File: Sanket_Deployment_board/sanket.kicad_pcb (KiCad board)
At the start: 2 copper layers, 95.9 x 92 mm, 41 parts, among them J2 Conn_02x03_Counter_Clockwise, J3 Conn_02x03_Counter_Clockwise

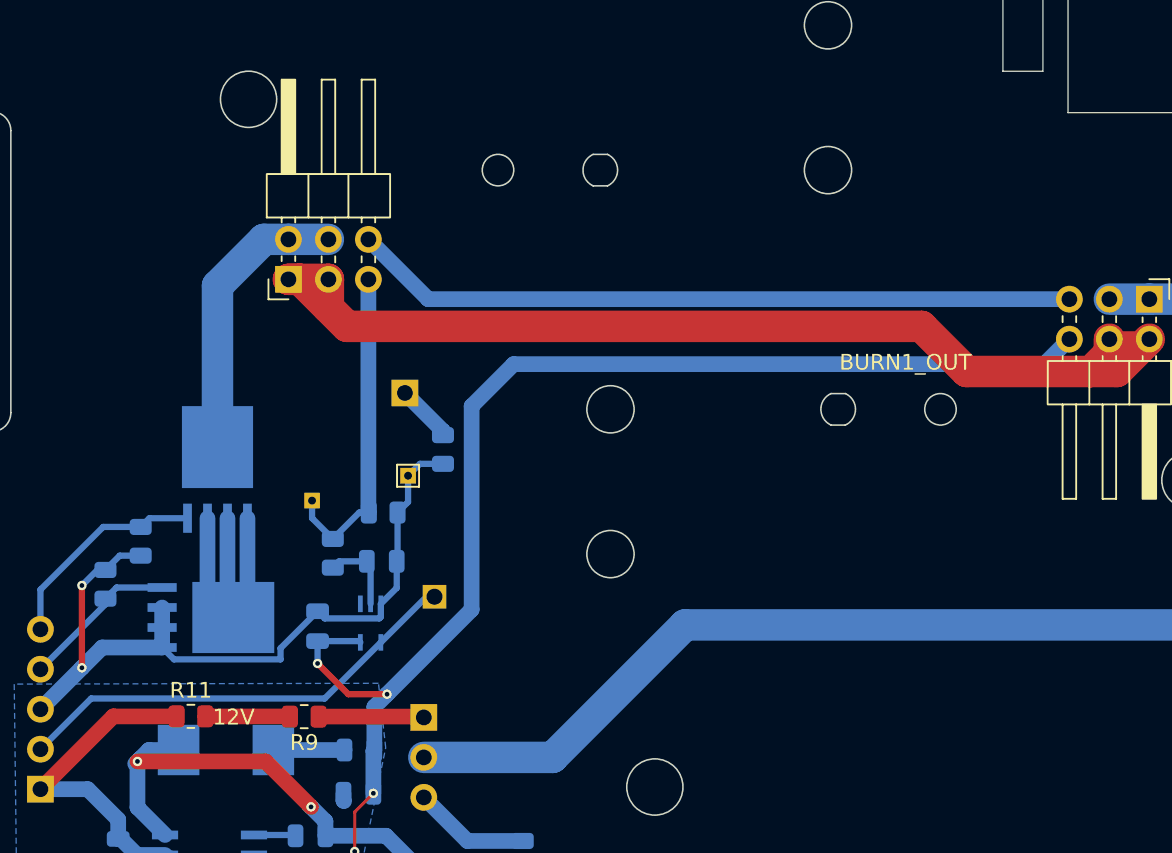
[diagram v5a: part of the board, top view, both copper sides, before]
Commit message: Added antenna bleeder, switched FIRE and ARM with each other, Corrected Schmitt trigger symbol to non-inverting
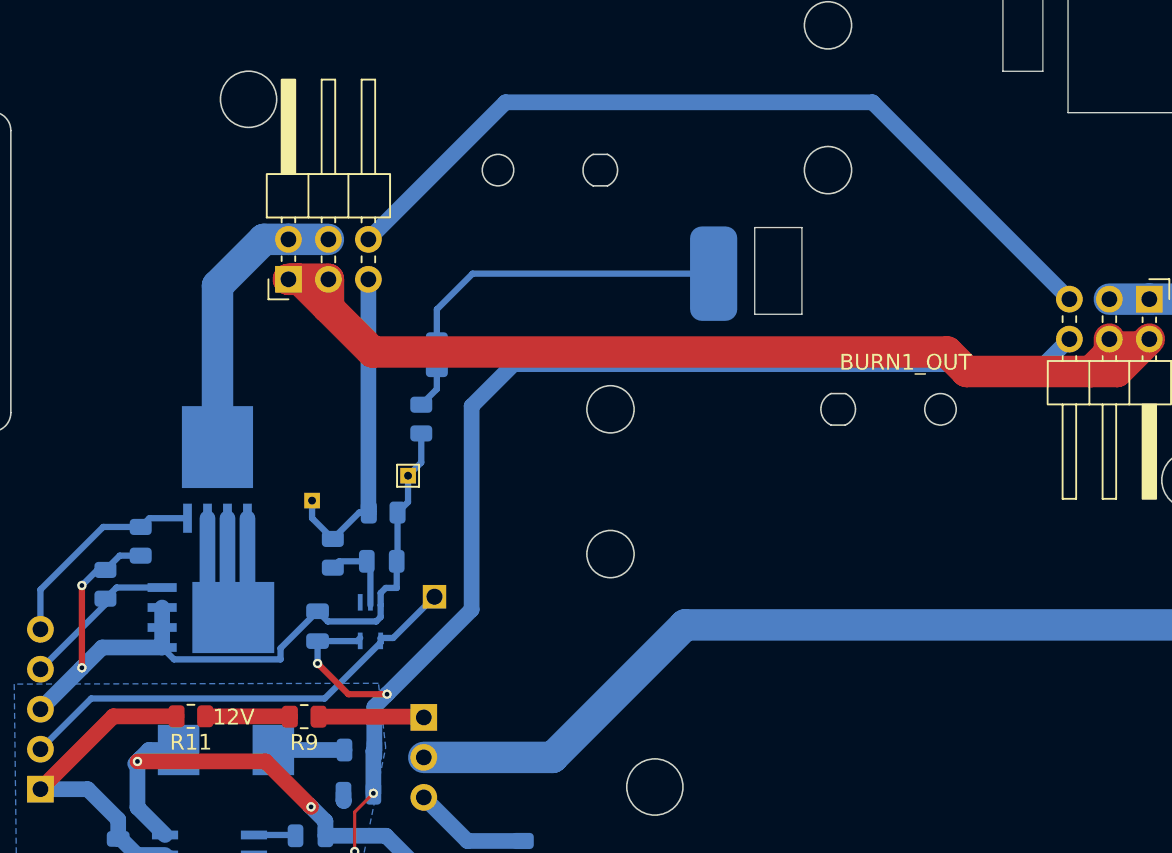
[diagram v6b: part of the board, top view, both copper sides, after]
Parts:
- removed U2: ~, Schmitt_trigger_ADS:DCK5-M
- added R13: 10M, Resistor_SMD:R_0805_2012Metric, B.Cu at (129.5, 111.5)
- added U1: SN74LVC1G17QDCKRQ1, Schmitt_trigger_ADS:DCK5-M, B.Cu at (126.3, 124.4)
- C3: value ~ -> 10n
- C9: value ~ -> 1800p
- J4: footprint Connector_PinSocket_2.54mm:PinSocket_1x01_P2.54mm_Vertical -> Connector_Wire:SolderWirePad_1x01_SMD_3x6mm
- R5: value ~ -> 10M
- moved J4 21.0 mm to (148.1, 102.3), turned to 0 degrees
- moved R5 6.04 mm to (130.5, 107.4)
- turned R11 to 180 degrees
- turned R3 to 90 degrees
- turned R4 to -90 degrees
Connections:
- net /3V3 renamed +3V3
- net /TriggerIN renamed Net-(U1-A)
- net Net-(J4-Pin_1) renamed /BLEEDER
- C10 pad 1: /12V -> +12V
- J8 pad 1: /12V -> +12V
- J8 pad 4: /FIRE -> /ARM
- J8 pad 5: /ARM -> /FIRE
- MOSFET1 pad 4: /ARM -> /FIRE
- MOSFET2 pad 4: /FIRE -> /ARM
- R11 pad 1: /12V -> Net-(R11-Pad1)
- R11 pad 2: Net-(R11-Pad2) -> +12V
- R3 pad 1: GND -> /ARM
- R3 pad 2: /FIRE -> GND
- R4 pad 1: GND -> /FIRE
- R4 pad 2: /ARM -> GND
- R5 pad 2: GND -> Net-(R13-Pad1)
- R9 pad 2: Net-(R11-Pad2) -> Net-(R11-Pad1)
- U3 pad 7: /12V -> +12V
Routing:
- net /12V: track 22.0 -> 0.00 mm
- net +12V: track 0.00 -> 22.0 mm
- net /BLEEDER: track 3.68 -> 20.5 mm
- net /DeployerDetectionSW1OUT: track 46.1 -> 53.3 mm
- net Net-(R11-Pad2): track 5.39 -> 0.00 mm
- net Net-(R11-Pad1): track 0.00 -> 5.39 mm
- net /FIRE: track 10.1 -> 13.9 mm
- net /ARM: track 13.9 -> 10.1 mm
- net Net-(R13-Pad1): track 0.00 -> 2.68 mm
- net GND: track 60.8 -> 61.9 mm
- net /TriggerOUT: track 29.1 -> 29.7 mm
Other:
- outline, holes or cut-outs redrawn
- board text added: "100p"
- board text added: "10M"

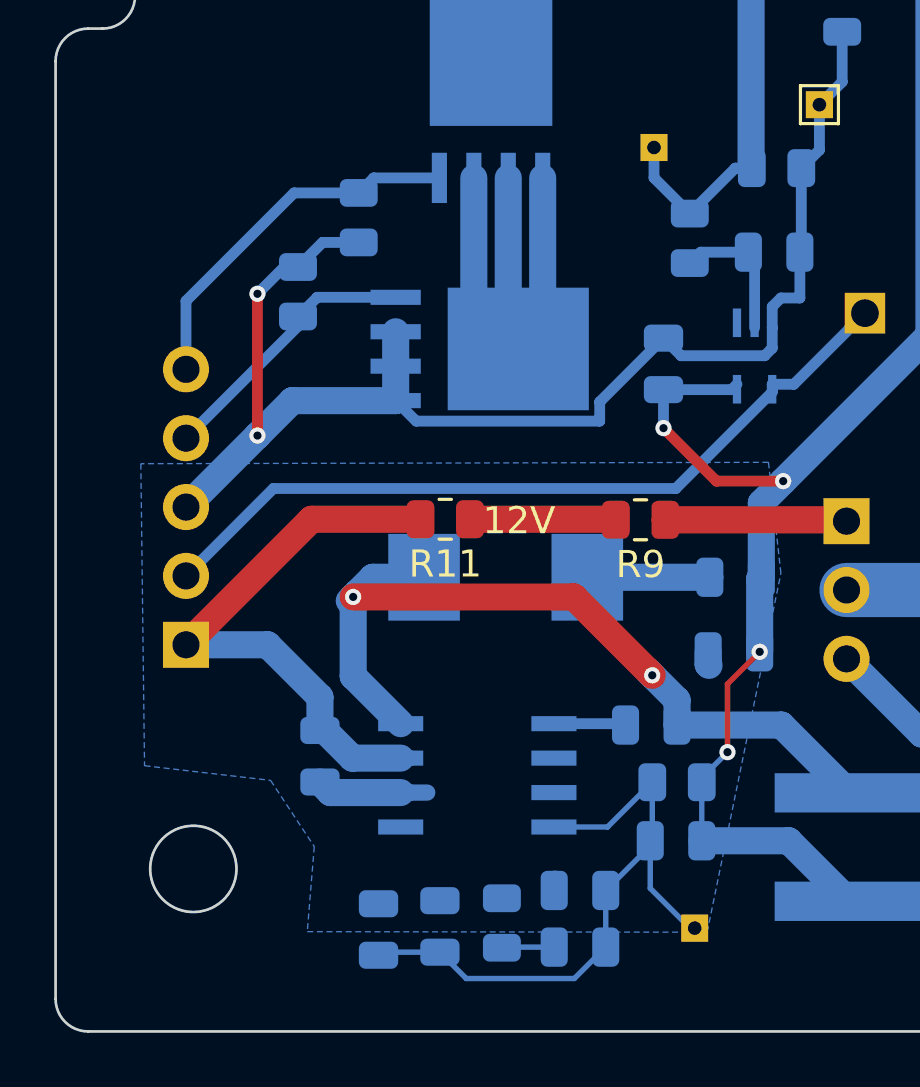
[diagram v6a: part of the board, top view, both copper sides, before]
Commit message: Replace a mounting hole to mounting pad to ground
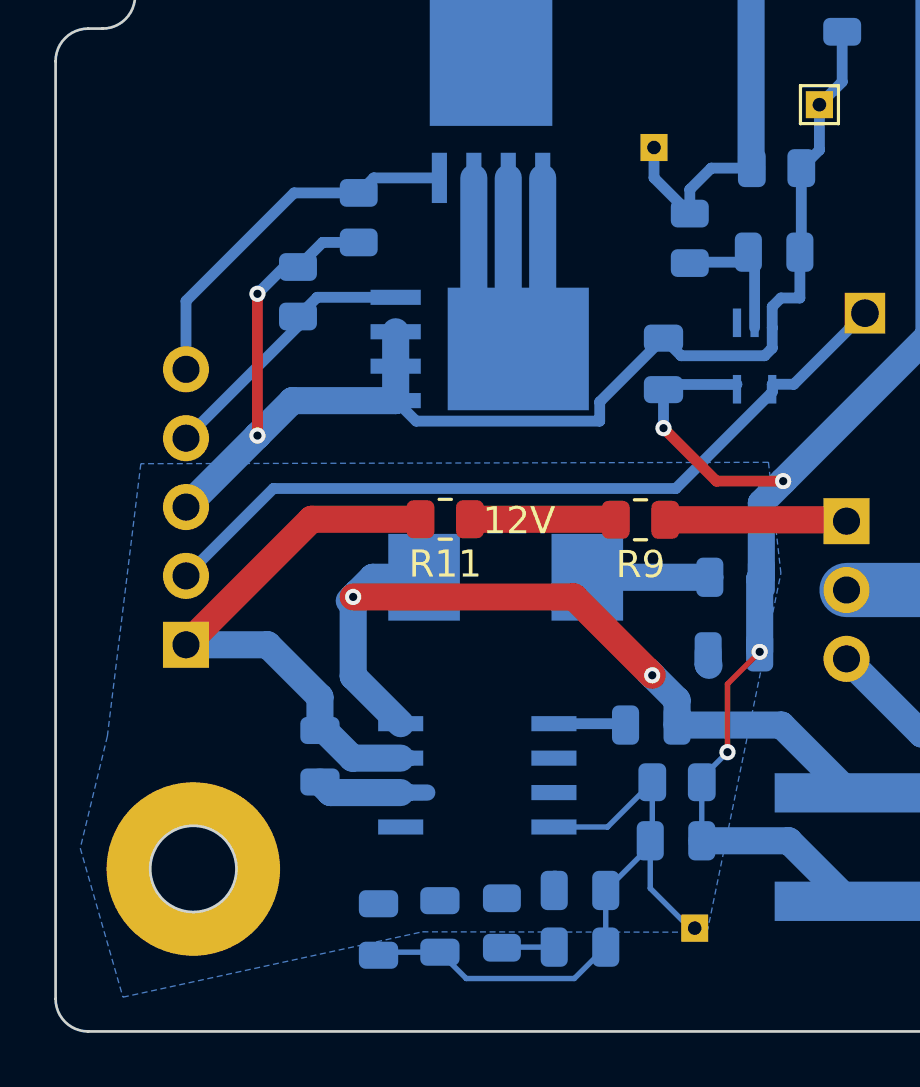
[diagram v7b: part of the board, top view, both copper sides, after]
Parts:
- H1: value ~ -> MountingHole_Pad; footprint MountingHole:MountingHole_3.2mm_M3 -> MountingHole:MountingHole_3.2mm_M3_Pad
- turned H1 to 0 degrees
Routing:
- net /DeployerDetectionSW2OUT: track 20.8 -> 21.3 mm
